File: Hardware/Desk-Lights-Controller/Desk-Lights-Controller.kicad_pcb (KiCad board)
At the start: 2 copper layers, 32 parts, among them J1 2604-1102, J2 2604-1102, J3 2604-1102, J4 2604-1103, K1 Relay_SPDT, K2 Relay_SPDT, Q1 BC817, Q2 BC817, U1 XIAO-SAMD21-SMD

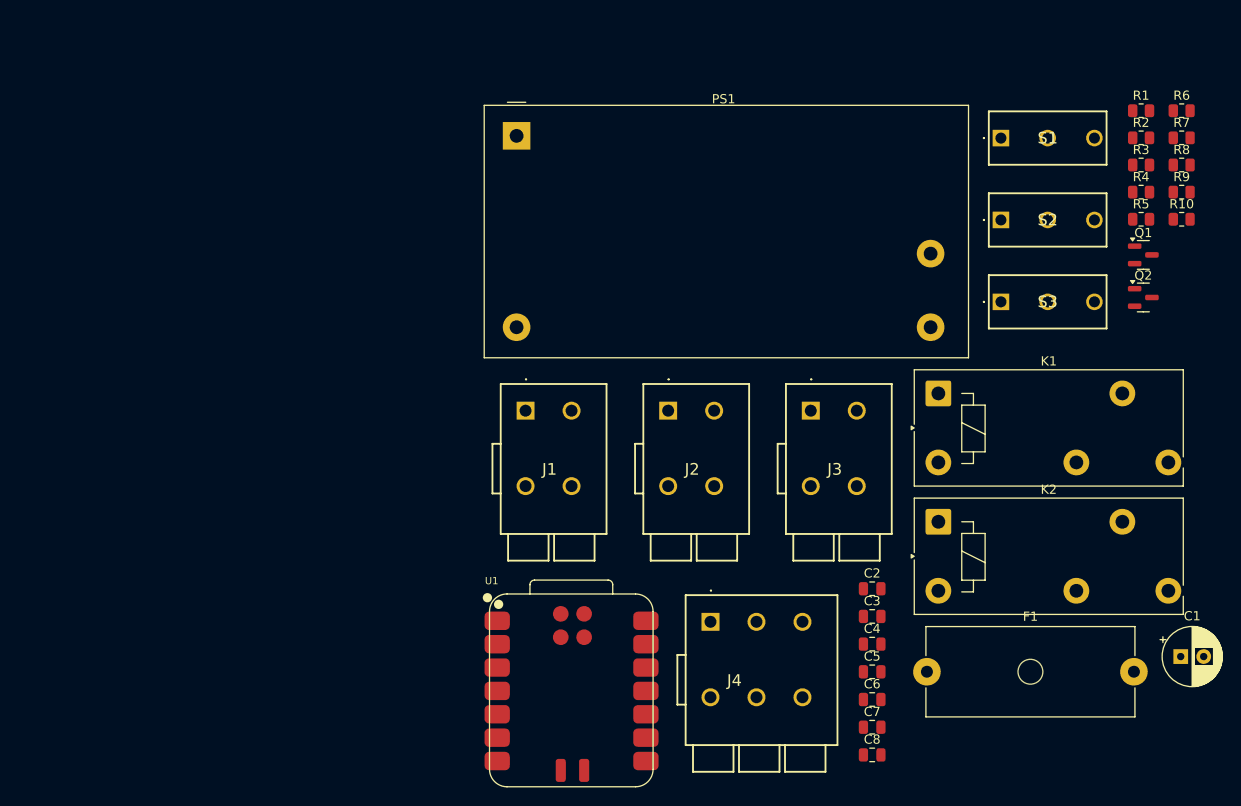
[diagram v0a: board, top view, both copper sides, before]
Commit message: Designed PCB, but it might be worth to shrink it a little bit
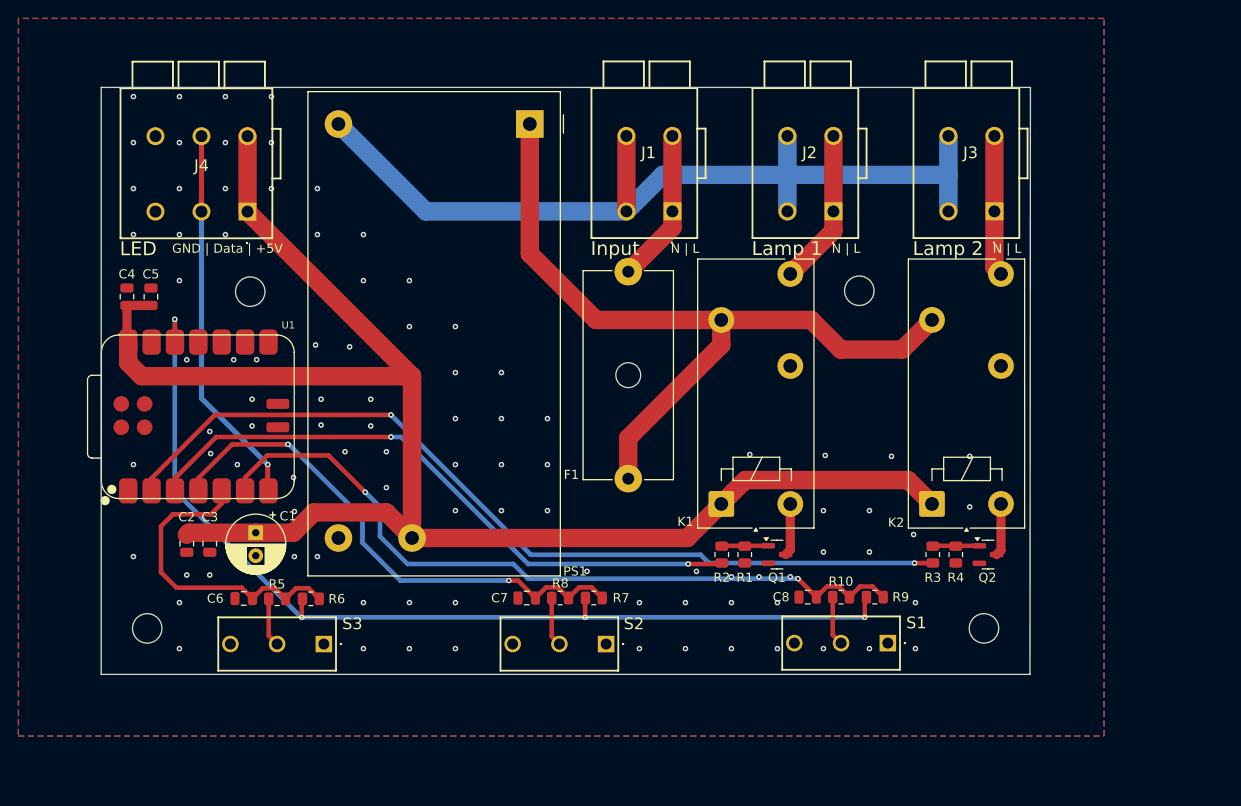
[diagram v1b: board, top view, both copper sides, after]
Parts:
- added H1: MountingHole, MountingHole:MountingHole_3.2mm_M3, F.Cu at (64.0, 120.3)
- added H2: MountingHole, MountingHole:MountingHole_3.2mm_M3, F.Cu at (154.9, 120.3)
- added H3: MountingHole, MountingHole:MountingHole_3.2mm_M3, F.Cu at (75.2, 83.7)
- added H4: MountingHole, MountingHole:MountingHole_3.2mm_M3, F.Cu at (141.4, 83.6)
- moved R6 108.5 mm to (81.8, 117.1), turned to 180 degrees
- moved R5 102.6 mm to (78.1, 117.1), turned to 180 degrees
- moved C1 101.4 mm to (75.8, 109.9), turned to -90 degrees
- moved C4 89.4 mm to (61.8, 84.2), turned to 90 degrees
- moved C5 88.4 mm to (64.4, 84.2), turned to 90 degrees
- moved S3 82.5 mm to (83.2, 122.0), turned to 180 degrees
- moved R8 82.3 mm to (108.9, 117.0), turned to 180 degrees
- moved R7 81.1 mm to (112.5, 117.0), turned to 180 degrees
- moved C2 74.7 mm to (68.3, 111.1), turned to -90 degrees
- moved C3 72.4 mm to (70.8, 111.1), turned to -90 degrees
- moved C6 69.2 mm to (74.5, 117.0), turned to 180 degrees
- moved J4 67.2 mm to (74.9, 75.0), turned to 180 degrees
- moved R1 64.7 mm to (128.9, 112.3), turned to -90 degrees
- moved R2 64.3 mm to (126.5, 112.3), turned to 90 degrees
- moved S2 63.0 mm to (113.9, 122.0), turned to 180 degrees
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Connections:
- R10 pad 2: GND -> Net-(S1-NO)
- S1 pad 2: GND -> Net-(S1-NO)
- U1 pad 5: /Button-3 -> /Button-2
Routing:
- net +5V: track 0.00 -> 178.3 mm
- net +3.3V: track 0.00 -> 108.3 mm, vias 0 -> 4
- net /N: track 0.00 -> 96.5 mm
- net /Lamp-1: track 0.00 -> 95.8 mm, vias 0 -> 2
- net /L-in: track 0.00 -> 84.9 mm
- net /Button-3: track 0.00 -> 82.0 mm, vias 0 -> 2
- net /Lamp-2: track 0.00 -> 68.4 mm, vias 0 -> 2
- net /Button-1: track 0.00 -> 57.2 mm, vias 0 -> 2
- net /Data: track 0.00 -> 41.6 mm, vias 0 -> 1
- net /Button-2: track 0.00 -> 34.3 mm
- net /L1-out: track 0.00 -> 16.9 mm
- net Net-(J1-1.1): track 0.00 -> 16.7 mm
- net /L2-out: track 0.00 -> 15.3 mm
- net Net-(Q1-C): track 0.00 -> 5.71 mm
- net Net-(Q2-C): track 0.00 -> 5.70 mm
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- added copper zone on B.Cu, net GND
- added copper zone on F.Cu, net GND
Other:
- board outline added: 101 x 63.8 mm
- board text added: "GND | Data | +5V"
- board text added: "Input"
- board text added: "LED"
- board text added: "Lamp 1"
- board text added: "Lamp 2"
- board text added: "N | L"
- board text added: "Szymon Wąchała Desk Lights Controller January 2025 v1.0"
